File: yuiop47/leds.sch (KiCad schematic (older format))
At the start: 1 part

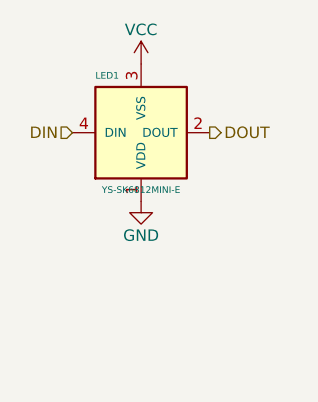
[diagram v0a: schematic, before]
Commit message: yuiop47: swap LED's VCC/GND
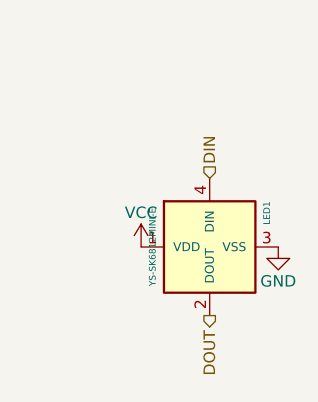
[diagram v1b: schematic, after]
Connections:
- net GND: now also LED1.3 (VSS); no longer LED1.1 (VDD)
- net VCC: now also LED1.1 (VDD); no longer LED1.3 (VSS)
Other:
- moved on the sheet: LED1
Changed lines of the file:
@@
 Sheet 2 3
 Title "YUIOP47/LEDs"
-Date "2021-01-19"
-Rev "1"
+Date "2021-01-26"
+Rev "2"
 Comp "KaoriYa"
 Comment1 ""
@@
 L power:VCC #PWR?
 U 1 1 603996F5
-P 5450 3950
+P 5450 4750
 AR Path="/603996F5" Ref="#PWR?"  Part="1"
 AR Path="/6000F835/603996F5" Ref="#PWR01"  Part="1"
@@
 AR Path="/6008B53F/603996F5" Ref="#PWR?"  Part="1"
 AR Path="/6008BE96/603996F5" Ref="#PWR?"  Part="1"
-F 0 "#PWR01" H 5450 3800 50  0001 C CNN
-F 1 "VCC" H 5450 4100 50  0000 C CNN
-F 2 "" H 5450 3950 50  0001 C CNN
-F 3 "" H 5450 3950 50  0001 C CNN
-	1    5450 3950
+F 0 "#PWR01" H 5450 4600 50  0001 C CNN
+F 1 "VCC" H 5450 4900 50  0000 C CNN
+F 2 "" H 5450 4750 50  0001 C CNN
+F 3 "" H 5450 4750 50  0001 C CNN
+	1    5450 4750
 	-1   0    0    -1
 $EndComp
@@
 L power:GND #PWR?
 U 1 1 603AFB72
-P 5450 4550
+P 6050 4750
 AR Path="/603AFB72" Ref="#PWR?"  Part="1"
 AR Path="/6000F835/603AFB72" Ref="#PWR02"  Part="1"
@@
 AR Path="/6008B53F/603AFB72" Ref="#PWR?"  Part="1"
 AR Path="/6008BE96/603AFB72" Ref="#PWR?"  Part="1"
-F 0 "#PWR02" H 5450 4300 50  0001 C CNN
-F 1 "GND" H 5450 4400 50  0000 C CNN
-F 2 "" H 5450 4550 50  0001 C CNN
-F 3 "" H 5450 4550 50  0001 C CNN
-	1    5450 4550
+F 0 "#PWR02" H 6050 4500 50  0001 C CNN
+F 1 "GND" H 6050 4600 50  0000 C CNN
+F 2 "" H 6050 4750 50  0001 C CNN
+F 3 "" H 6050 4750 50  0001 C CNN
+	1    6050 4750
 	-1   0    0    -1
 $EndComp
@@
 L kbd:YS-SK6812MINI-E LED?
 U 1 1 601A5A84
-P 5450 4250
+P 5750 4750
 AR Path="/601A5A84" Ref="LED?"  Part="1"
 AR Path="/6000F835/601A5A84" Ref="LED1"  Part="1"
@@
 AR Path="/6008B53F/601A5A84" Ref="LED?"  Part="1"
 AR Path="/6008BE96/601A5A84" Ref="LED?"  Part="1"
-F 0 "LED1" H 5250 4000 29  0000 L CNN
-F 1 "YS-SK6812MINI-E" H 5450 4500 29  0000 C CNN
-F 2 "yuiop:SK6812MINI-E_B" H 5550 4000 50  0001 C CNN
-F 3 "" H 5550 4000 50  0001 C CNN
-	1    5450 4250
-	1    0    0    1
+F 0 "LED1" H 5550 4500 29  0000 L CNN
+F 1 "YS-SK6812MINI-E" H 5750 5000 29  0000 C CNN
+F 2 "yuiop:SK6812MINI-E_B" H 5850 4500 50  0001 C CNN
+F 3 "" H 5850 4500 50  0001 C CNN
+	1    5750 4750
+	0    -1   1    0
 $EndComp
-Text HLabel 5150 4250 0    50   Input ~ 0
+Text HLabel 5750 4450 1    50   Input ~ 0
 DIN
-Text HLabel 5750 4250 2    50   Output ~ 0
+Text HLabel 5750 5050 3    50   Output ~ 0
 DOUT
 $EndSCHEMATC
